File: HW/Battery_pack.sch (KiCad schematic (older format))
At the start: 3 parts

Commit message: add footprint of battery pack
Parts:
- U?: footprint (none) -> my_library:battery_dock
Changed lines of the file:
@@
 F 0 "U?" H 4400 2505 50  0000 C CNN
 F 1 "Dual_battery" H 4400 2414 50  0000 C CNN
-F 2 "" H 4400 2100 50  0001 C CNN
+F 2 "my_library:battery_dock" H 4400 2100 50  0001 C CNN
 F 3 "" H 4400 2100 50  0001 C CNN
 	1    4400 2100

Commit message: add footprint of inductor, add codes for JLCPCB, repair mistakes
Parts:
- F? (x2): footprint (none) -> Fuse:Fuse_0603_1608Metric; LCSC (none) -> C20792
- U?: LCSC (none) -> ručně
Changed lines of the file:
@@
 F 0 "F?" V 3575 1950 50  0000 C CNN
 F 1 "Polyfuse" V 3666 1950 50  0000 C CNN
-F 2 "" H 3850 1750 50  0001 L CNN
+F 2 "Fuse:Fuse_0603_1608Metric" H 3850 1750 50  0001 L CNN
 F 3 "~" H 3800 1950 50  0001 C CNN
+F 4 "C20792" H 3800 1950 50  0001 C CNN "LCSC"
 	1    3800 1950
 	0    1    1    0
@@
 F 0 "F?" V 3575 2250 50  0000 C CNN
 F 1 "Polyfuse" V 3666 2250 50  0000 C CNN
-F 2 "" H 3850 2050 50  0001 L CNN
+F 2 "Fuse:Fuse_0603_1608Metric" H 3850 2050 50  0001 L CNN
 F 3 "~" H 3800 2250 50  0001 C CNN
+F 4 "C20792" H 3800 2250 50  0001 C CNN "LCSC"
 	1    3800 2250
 	0    1    1    0
@@
 F 2 "my_library:battery_dock" H 4400 2100 50  0001 C CNN
 F 3 "" H 4400 2100 50  0001 C CNN
+F 4 "ručně" H 4400 2100 50  0001 C CNN "LCSC"
 	1    4400 2100
 	1    0    0    -1

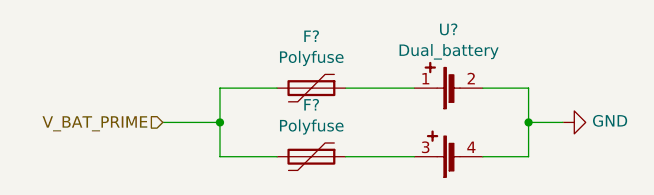
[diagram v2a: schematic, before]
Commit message: numbering components, place components on board
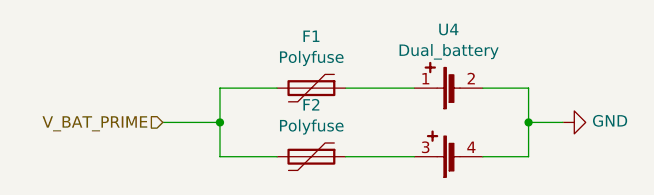
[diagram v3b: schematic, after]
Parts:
- gave numbers to parts that had none: 3
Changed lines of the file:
@@
 $EndDescr
 $Comp
-L power:GND #PWR?
+L power:GND #PWR0140
 U 1 1 5F74BC2B
 P 4900 2100
-F 0 "#PWR?" H 4900 1850 50  0001 C CNN
+F 0 "#PWR0140" H 4900 1850 50  0001 C CNN
 F 1 "GND" V 4905 1972 50  0000 R CNN
 F 2 "" H 4900 2100 50  0001 C CNN
@@
 V_BAT_PRIME
 $Comp
-L Device:Polyfuse F?
+L Device:Polyfuse F1
 U 1 1 5F77C417
 P 3800 1950
-F 0 "F?" V 3575 1950 50  0000 C CNN
+F 0 "F1" V 3575 1950 50  0000 C CNN
 F 1 "Polyfuse" V 3666 1950 50  0000 C CNN
 F 2 "Fuse:Fuse_0603_1608Metric" H 3850 1750 50  0001 L CNN
@@
 $EndComp
 $Comp
-L Device:Polyfuse F?
+L Device:Polyfuse F2
 U 1 1 5F77C5DC
 P 3800 2250
-F 0 "F?" V 3575 2250 50  0000 C CNN
+F 0 "F2" V 3575 2250 50  0000 C CNN
 F 1 "Polyfuse" V 3666 2250 50  0000 C CNN
 F 2 "Fuse:Fuse_0603_1608Metric" H 3850 2050 50  0001 L CNN
@@
 $EndComp
 $Comp
-L symbols:Dual_battery U?
+L symbols:Dual_battery U4
 U 1 1 5F8A8975
 P 4400 2100
-F 0 "U?" H 4400 2505 50  0000 C CNN
+F 0 "U4" H 4400 2505 50  0000 C CNN
 F 1 "Dual_battery" H 4400 2414 50  0000 C CNN
 F 2 "my_library:battery_dock" H 4400 2100 50  0001 C CNN
